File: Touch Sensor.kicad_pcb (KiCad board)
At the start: 2 copper layers, 1 part

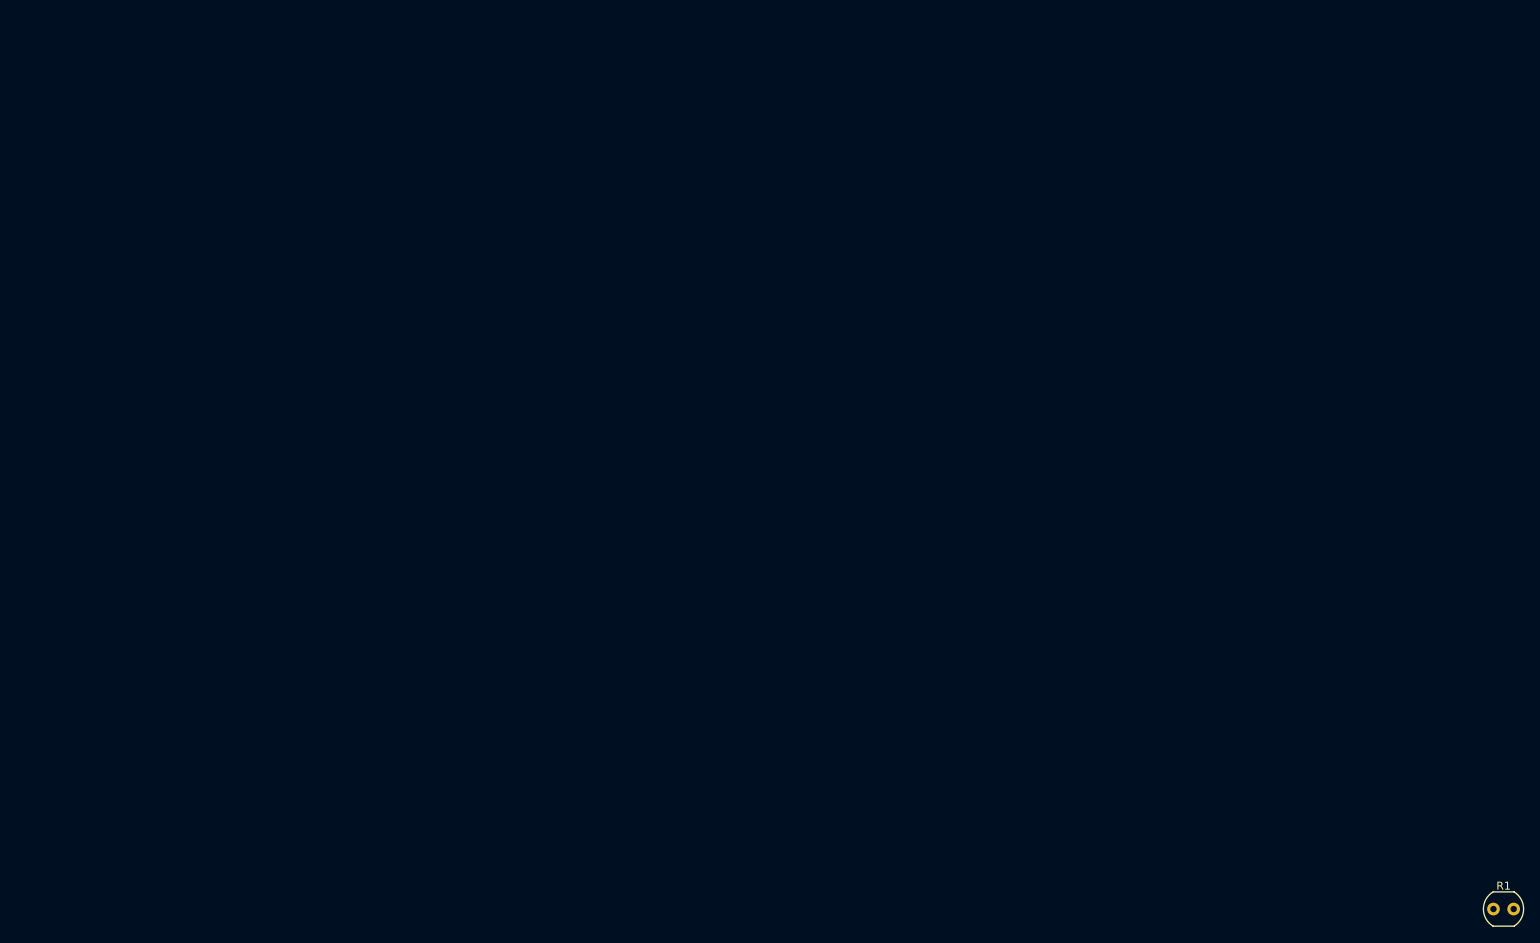
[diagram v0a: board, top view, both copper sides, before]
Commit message: added 3MHz gen and touch sensor circuit
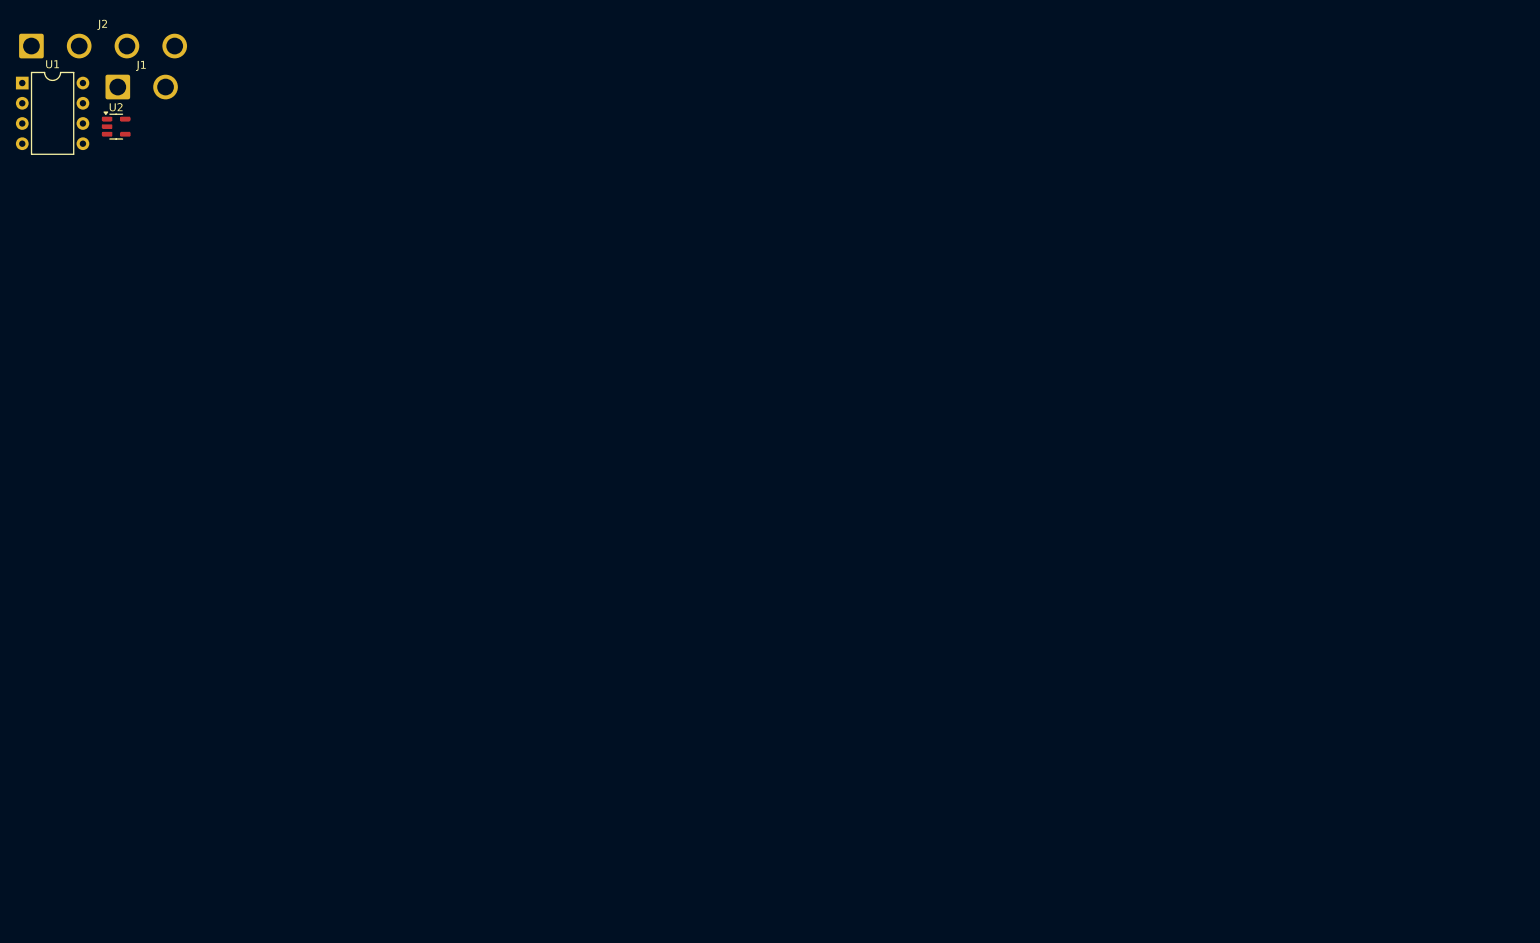
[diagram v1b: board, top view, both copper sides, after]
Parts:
- removed R1: R, OptoDevice:R_LDR_4.9x4.2mm_P2.54mm_Vertical
- added J1: Conn_01x02_Pin, Connector_Wire:SolderWire-1.5sqmm_1x02_P6mm_D1.7mm_OD3mm, F.Cu at (13.1, 7.22)
- added J2: Conn_01x04_Pin, Connector_Wire:SolderWire-1.5sqmm_1x04_P6mm_D1.7mm_OD3mm, F.Cu at (2.27, 2.08)
- added U1: LMC555xN, Package_DIP:DIP-8_W7.62mm, F.Cu at (1.12, 6.72)
- added U2: SN74LVC1G14DBV, Package_TO_SOT_SMD:SOT-23-5, F.Cu at (12.9, 12.2)
